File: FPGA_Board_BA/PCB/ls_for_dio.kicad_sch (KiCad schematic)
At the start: 5 parts, among them U36 SN74LXC2T45Q1

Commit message: exported stuff
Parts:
- renumbered C148 to C143, C149 to C144, R179 to R218, R180 to R219, U36 to U35
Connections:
- net +1V8: now also R218.1, R219.1
- net +3.3V: no longer R218.1, R219.1
- net A1: now also R218.2
- net A2: now also R219.2
- net B1: no longer R218.2
- net B2: no longer R219.2
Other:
- moved on the sheet: R218, R219

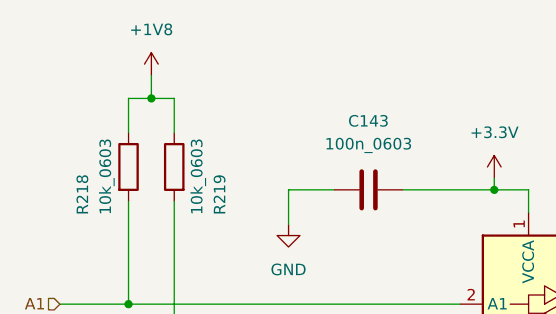
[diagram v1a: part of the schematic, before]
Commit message: optimised pinout in schematic + added level shifter for CLKOUT + got forward with layout
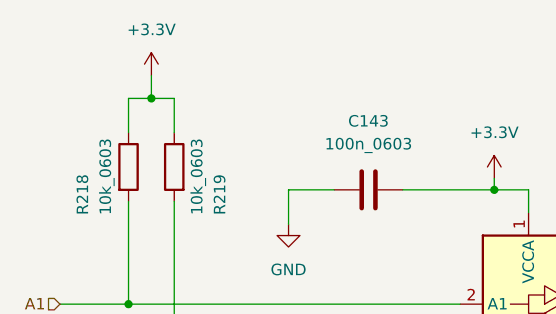
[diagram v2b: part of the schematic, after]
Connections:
- net +1V8: no longer R218.1, R219.1
- net +3.3V: now also R218.1, R219.1
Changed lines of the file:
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@@
-	)
-	(symbol
-		(lib_id "power:+1V8")
-		(at 86.36 67.31 0)
-		(unit 1)
-		(exclude_from_sim no)
-		(in_bom yes)
-		(on_board yes)
-		(dnp no)
-		(fields_autoplaced yes)
-		(property "Reference" "#PWR0231"
-			(at 86.36 71.12 0)
-			(effects
-				(font
-					(size 1.27 1.27)
-				)
-				(hide yes)
-			)
-		)
-		(property "Value" "+1V8"
-			(at 86.36 62.23 0)
-			(effects
-				(font
-					(size 1.27 1.27)
-				)
-			)
-		)
-		(property "Footprint" ""
-			(at 86.36 67.31 0)
-			(effects
-				(font
-					(size 1.27 1.27)
-				)
-				(hide yes)
-			)
-		)
-		(property "Datasheet" ""
-			(at 86.36 67.31 0)
-			(effects
-				(font
-					(size 1.27 1.27)
-				)
-				(hide yes)
-			)
-		)
-		(property "Description" "Power symbol creates a global label with name \"+1V8\""
-			(at 86.36 67.31 0)
-			(effects
-				(font
-					(size 1.27 1.27)
-				)
-				(hide yes)
-			)
-		)
-		(pin "1"
-		)
-		(instances
-			(project "FPGA_Board_BA"
-				(path "/fd7503bc-e7fc-4766-b224-3d1c3d7de5ff/61f82991-823e-4c29-9a78-9b2ec5b110b2/90f23285-27cc-4590-a3de-f3bed661e97d"
-					(reference "#PWR0265")
-					(unit 1)
-				)
-				(path "/fd7503bc-e7fc-4766-b224-3d1c3d7de5ff/b651456b-f82d-416a-adc2-766f971f7bfa/3aef2b1a-46e4-4d2a-8508-77241448084f"
-					(reference "#PWR0231")
-					(unit 1)
-				)
-			)
-		)
 	)
 	(symbol
@@
 					(unit 1)
 				)
+			)
+		)
+	)
+	(symbol
+		(lib_id "power:+3.3V")
+		(at 86.36 67.31 0)
+		(unit 1)
+		(exclude_from_sim no)
+		(in_bom yes)
+		(on_board yes)
+		(dnp no)
+		(fields_autoplaced yes)
+		(property "Reference" "#PWR0135"
+			(at 86.36 71.12 0)
+			(effects
+				(font
+					(size 1.27 1.27)
+				)
+				(hide yes)
+			)
+		)
+		(property "Value" "+3.3V"
+			(at 86.36 62.23 0)
+			(effects
+				(font
+					(size 1.27 1.27)
+				)
+			)
+		)
+		(property "Footprint" ""
+			(at 86.36 67.31 0)
+			(effects
+				(font
+					(size 1.27 1.27)
+				)
+				(hide yes)
+			)
+		)
+		(property "Datasheet" ""
+			(at 86.36 67.31 0)
+			(effects
+				(font
+					(size 1.27 1.27)
+				)
+				(hide yes)
+			)
+		)
+		(property "Description" "Power symbol creates a global label with name \"+3.3V\""
+			(at 86.36 67.31 0)
+			(effects
+				(font
+					(size 1.27 1.27)
+				)
+				(hide yes)
+			)
+		)
+		(pin "1"
+		)
+		(instances
+			(project "FPGA_Board_BA"
+				(path "/fd7503bc-e7fc-4766-b224-3d1c3d7de5ff/61f82991-823e-4c29-9a78-9b2ec5b110b2/90f23285-27cc-4590-a3de-f3bed661e97d"
+					(reference "#PWR0140")
+					(unit 1)
+				)
+				(path "/fd7503bc-e7fc-4766-b224-3d1c3d7de5ff/b651456b-f82d-416a-adc2-766f971f7bfa/3aef2b1a-46e4-4d2a-8508-77241448084f"
+					(reference "#PWR0135")
+					(unit 1)
+				)
